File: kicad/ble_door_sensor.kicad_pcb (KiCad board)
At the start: 4 copper layers, 20 x 61.5 mm, 38 parts, among them J1 Prog Header, J101 Conn_01x08, SW101 SW_Reed, SW102 SW_Push, U1 nRF52832-QFxx, U101 TMP100, Y1 Crystal_GND24

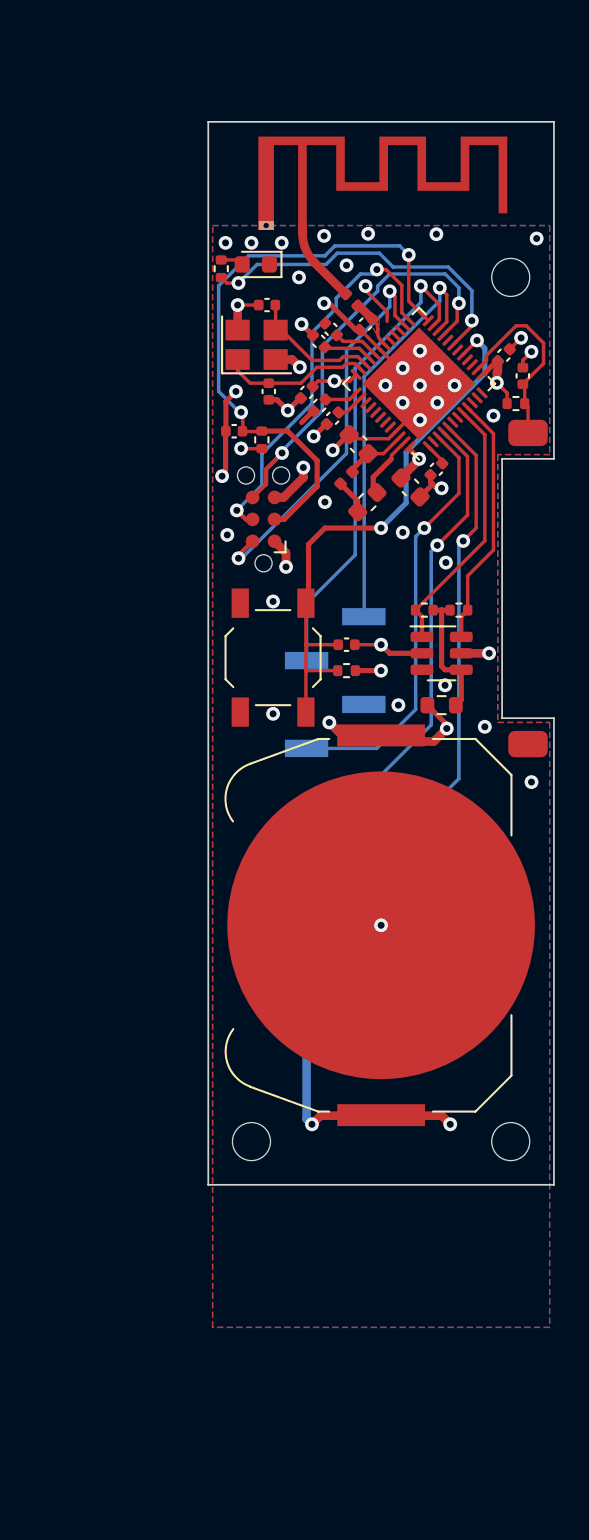
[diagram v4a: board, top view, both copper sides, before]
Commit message: Add tmp100 sensor for temperature
also added mounting holes for assembly machines
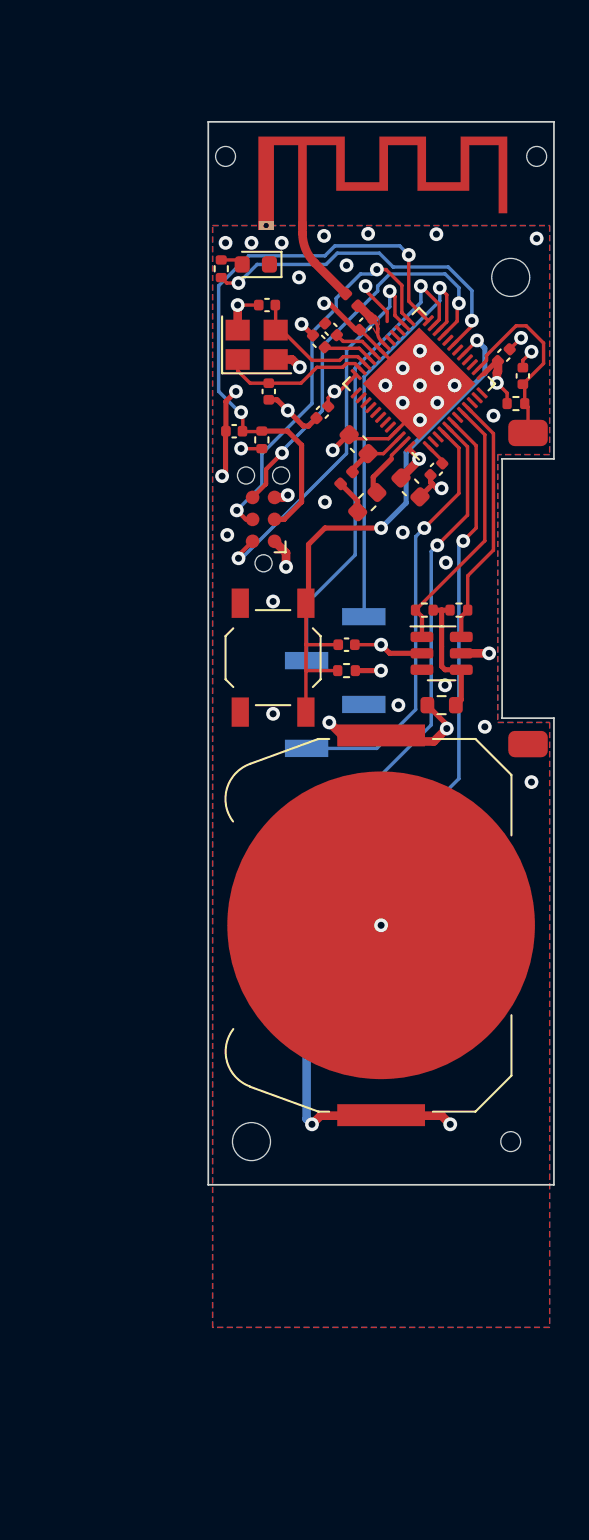
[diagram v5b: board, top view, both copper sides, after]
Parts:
- removed C105, C106: 12pF, Capacitor_SMD:C_0402_1005Metric
- removed H103: MountingHole, MountingHole:MountingHole_2.2mm_M2
- added T1: ToolingHole, Library:JLCPCB_Mounting_hole, F.Cu at (126.0, 42.0)
- added T2: ToolingHole, Library:JLCPCB_Mounting_hole, F.Cu at (142.5, 99.0)
- added T3: ToolingHole, Library:JLCPCB_Mounting_hole, F.Cu at (144.0, 42.0)
- moved C107 1.46 mm to (131.6, 56.8)
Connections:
- U1 pad 3: P0.01 -> unconnected-(U1-P0.01/XL2-Pad3)
- U1 pad 37: Net-(U1-P0.25) -> unconnected-(U1-P0.25-Pad37)
- U1 pad 38: Net-(U1-P0.26) -> unconnected-(U1-P0.26-Pad38)
- U1 pad 4: P0.02 -> P0.01
- U1 pad 5: P0.03 -> P0.02
- U1 pad 6: unconnected-(U1-P0.04/AIN2-Pad6) -> P0.03
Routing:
- net GND: track 66.2 -> 63.4 mm, vias 46 -> 45
- net Net-(U1-P0.25): track 1.93 -> 0.00 mm
- net Net-(U1-P0.26): track 1.65 -> 0.00 mm
- net RESET: track 35.3 -> 34.5 mm
- net P0.01: track 24.6 -> 25.2 mm

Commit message: Add ambient light and humidity sensor
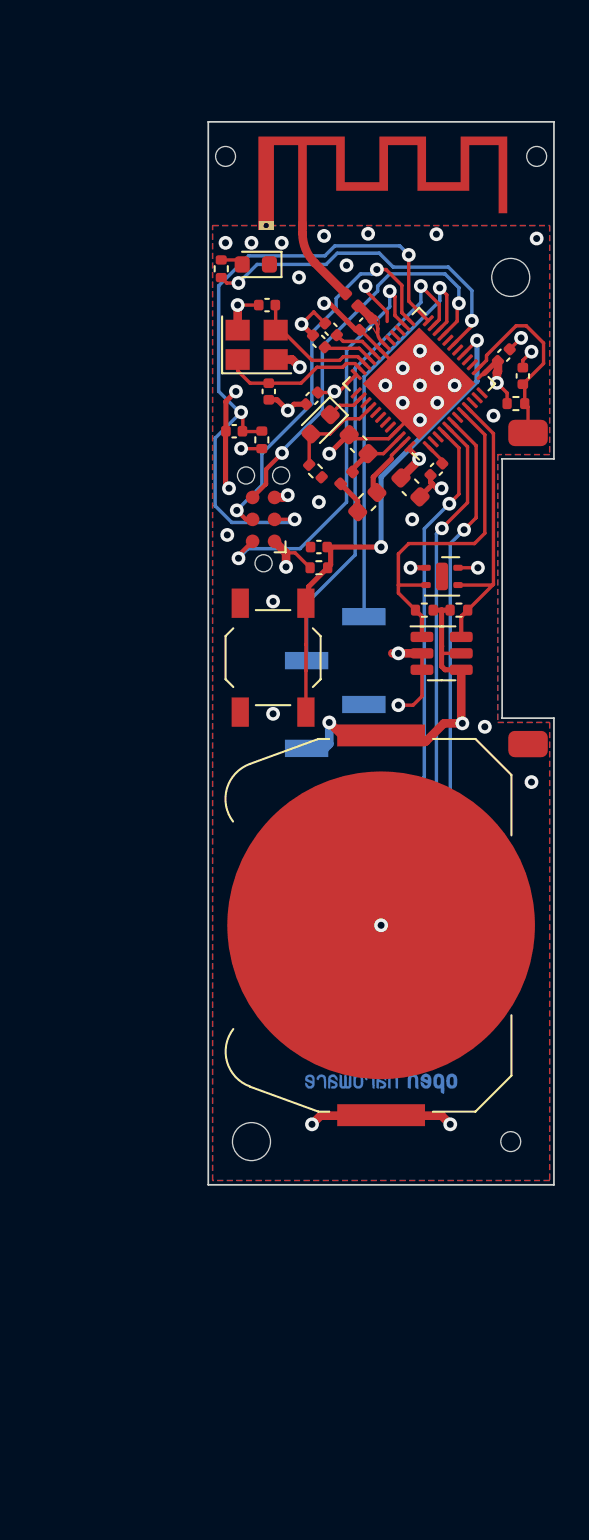
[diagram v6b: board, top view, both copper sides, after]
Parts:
- removed R103: 0, Resistor_SMD:R_0603_1608Metric
- added Q1: Photo, LED_SMD:LED_0603_1608Metric, F.Cu at (131.5, 57.5)
- added R3: 1K, Resistor_SMD:R_0402_1005Metric, F.Cu at (131.2, 60.2)
- added REF**: OSHW-Logo2_9.8x8mm_Copper, Symbol:OSHW-Logo2_9.8x8mm_Copper, B.Cu at (135.0, 92.5)
- added U2: SHTC3, Sensor_Humidity:Sensirion_DFN-4-1EP_2x2mm_P1mm_EP0.7x1.6mm, F.Cu at (138.5, 66.3)
- moved R101 6.16 mm to (131.4, 65.8), turned to 0 degrees
- moved C101 5.87 mm to (131.4, 64.6), turned to 180 degrees
- moved C107 1.00 mm to (131.0, 56.0)
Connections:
- J101 pad 4: P0.01 -> VCC
- J101 pad 5: P0.02 -> P0.01
- J101 pad 6: P0.03 -> P0.02
- J101 pad 7: GND -> P0.03
- J101 pad 8: VCC -> GND
- R104 pad 1: /VCC_Temp -> VCC
- R105 pad 1: /VCC_Temp -> VCC
- U1 pad 38: unconnected-(U1-P0.26-Pad38) -> /Photo_out
- U1 pad 40: unconnected-(U1-P0.28/AIN4-Pad40) -> /Photo_in
- U101 pad 4: /VCC_Temp -> VCC
- U101 pad 5: GND -> VCC
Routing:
- net GND: track 63.4 -> 71.2 mm, vias 45 -> 43
- net /VCC_Temp: track 7.63 -> 0.00 mm
- net P0.02: track 24.1 -> 31.1 mm
- net /Photo_in: track 0.00 -> 5.92 mm
- net SCL: track 15.3 -> 20.0 mm
- net RESET: track 34.5 -> 38.9 mm, vias 2 -> 3
- net BUTTON: track 32.8 -> 28.5 mm
- net /Photo_out: track 0.00 -> 2.19 mm
- net SDA: track 14.7 -> 16.7 mm
- net SWDIO: track 22.9 -> 24.5 mm
- net VCC: track 43.1 -> 44.1 mm

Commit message: Add MPN and Manufacturer for most parts
To be able to order from different houses
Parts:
- BT1: value Battery_Cell -> 3034
- Q1: value Photo -> ALS-PT19
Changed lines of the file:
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@@
     (tags "SMD SMT crystal")
     (property "LCSC#" "C9009")
+    (property "MPN" "X322532MOB4SI")
+    (property "Manufacturer" "YXC")
     (property "Sheetfile" "ble_door_sensor.kicad_sch")
     (property "Sheetname" "")
@@
     (tags "capacitor")
     (property "LCSC#" "C15195")
+    (property "MPN" "10nF 0402")
     (property "Sheetfile" "ble_door_sensor.kicad_sch")
     (property "Sheetname" "")
@@
   (footprint "Library:JLCPCB_Mounting_hole" (layer "F.Cu")
     (at 144 42)
+    (property "LCSC#" "-")
+    (property "MPN" "-")
     (property "Sheetfile" "ble_door_sensor.kicad_sch")
     (property "Sheetname" "")
+    (property "exclude_from_bom" "")
     (property "ki_description" "Mounting Hole without connection")
     (property "ki_keywords" "mounting hole")
+    (attr exclude_from_pos_files exclude_from_bom)
     (fp_text reference "T3" (at 0 -2.032 unlocked) (layer "F.SilkS") hide
         (effects (font (size 1 1) (thickness 0.1)))
@@
     (tags "mounting hole 2.2mm no annular m2")
     (property "LCSC#" "-")
+    (property "MPN" "-")
     (property "Sheetfile" "ble_door_sensor.kicad_sch")
     (property "Sheetname" "")
@@
     (tags "QFN NoLead")
     (property "LCSC#" "C77540")
+    (property "MPN" "NRF52832-QFAA-R")
+    (property "Manufacturer" "Nordic Semicon")
     (property "Sheetfile" "ble_door_sensor.kicad_sch")
     (property "Sheetname" "")
@@
     (tags "capacitor")
     (property "LCSC#" "C1525")
+    (property "MPN" "100nF 0402")
     (property "Sheetfile" "ble_door_sensor.kicad_sch")
     (property "Sheetname" "")
@@
     (tags "capacitor")
     (property "LCSC#" "C1546")
+    (property "MPN" "100pF 0402")
     (property "Sheetfile" "ble_door_sensor.kicad_sch")
     (property "Sheetname" "")
@@
     (tags "capacitor")
     (property "LCSC#" "C15849")
+    (property "MPN" "1uF 0603")
     (property "Sheetfile" "ble_door_sensor.kicad_sch")
     (property "Sheetname" "")
@@
     (at 143.5 67)
     (property "LCSC#" "-")
+    (property "MPN" "-")
     (property "Sheetfile" "ble_door_sensor.kicad_sch")
     (property "Sheetname" "")
@@
     (tags "inductor")
     (property "LCSC#" "C1035")
+    (property "MPN" "MLZ1608E100MT")
+    (property "Manufacturer" "TDK")
     (property "Sheetfile" "ble_door_sensor.kicad_sch")
     (property "Sheetname" "")
@@
     (tags "Keystone type 3034 coin cell retainer")
     (property "LCSC#" "C5213768")
+    (property "MPN" "3034TR")
+    (property "Manufacturer" "Keystone")
     (property "Sheetfile" "ble_door_sensor.kicad_sch")
     (property "Sheetname" "")
@@
         (effects (font (size 1 1) (thickness 0.15)))
     )
-    (fp_text value "Battery_Cell" (at 0 11.5 90) (layer "F.Fab")
+    (fp_text value "3034" (at 0 11.5 90) (layer "F.Fab")
         (effects (font (size 1 1) (thickness 0.15)))
     )
@@
     (tags "resistor")
     (property "LCSC#" "C11702")
+    (property "MPN" "1K")
     (property "Sheetfile" "ble_door_sensor.kicad_sch")
     (property "Sheetname" "")
@@
     (tags "capacitor")
     (property "LCSC#" "C1547")
+    (property "MPN" "12pF 0402")
     (property "Sheetfile" "ble_door_sensor.kicad_sch")
     (property "Sheetname" "")
@@
     (tags "resistor")
     (property "LCSC#" "C11702")
+    (property "MPN" "1K")
     (property "Sheetfile" "ble_door_sensor.kicad_sch")
     (property "Sheetname" "")
@@
     (tags "LED")
     (property "LCSC#" "C72043")
+    (property "MPN" " KP-1608SGC")
     (property "Sheetfile" "ble_door_sensor.kicad_sch")
     (property "Sheetname" "")
@@
     (tags "resistor")
     (property "LCSC#" "C25741")
+    (property "MPN" "100K")
     (property "Sheetfile" "ble_door_sensor.kicad_sch")
     (property "Sheetname" "")
@@
     (tags "mounting hole 2.2mm no annular m2")
     (property "LCSC#" "-")
+    (property "MPN" "-")
     (property "Sheetfile" "ble_door_sensor.kicad_sch")
     (property "Sheetname" "")
@@
     (tags "Sensirion DFN NoLead")
     (property "LCSC#" "C2880044")
+    (property "MPN" "SHTC3-TR-10KS")
+    (property "Manufacturer" "Sensirion")
     (property "Sheetfile" "ble_door_sensor.kicad_sch")
     (property "Sheetname" "")
@@
     (tags "resistor")
     (property "LCSC#" "C26083")
+    (property "MPN" "1M")
     (property "Sheetfile" "ble_door_sensor.kicad_sch")
     (property "Sheetname" "")
@@
     (tags "resistor")
     (property "LCSC#" "C25741")
+    (property "MPN" "100K")
     (property "Sheetfile" "ble_door_sensor.kicad_sch")
     (property "Sheetname" "")
@@
     (tags "capacitor")
     (property "LCSC#" "C1525")
+    (property "MPN" "100nF 0402")
     (property "Sheetfile" "ble_door_sensor.kicad_sch")
     (property "Sheetname" "")
@@
     (tags "capacitor")
     (property "LCSC#" "-")
+    (property "MPN" "-")
     (property "Sheetfile" "ble_door_sensor.kicad_sch")
     (property "Sheetname" "")
@@
     (property "ki_description" "Unpolarized capacitor, small symbol")
     (property "ki_keywords" "capacitor cap")
-    (attr smd exclude_from_bom)
+    (attr smd exclude_from_pos_files exclude_from_bom)
     (fp_text reference "C4" (at 0 -1.16 45) (layer "F.SilkS") hide
         (effects (font (size 1 1) (thickness 0.15)))
@@
     (tags "capacitor")
     (property "LCSC#" "C1525")
+    (property "MPN" "100nF 0402")
     (property "Sheetfile" "ble_door_sensor.kicad_sch")
     (property "Sheetname" "")
@@
     (tags "PCB antenna")
     (property "LCSC#" "-")
+    (property "MPN" "-")
     (property "Sheetfile" "ble_door_sensor.kicad_sch")
     (property "Sheetname" "")
@@
     (tags "SOT TO_SOT_SMD")
     (property "LCSC#" "C31810")
+    (property "MPN" "TMP100NA/3K")
+    (property "Manufacturer" "Texas Instruments")
     (property "Sheetfile" "ble_door_sensor.kicad_sch")
     (property "Sheetname" "")
@@
     (tags "capacitor")
     (property "LCSC#" "C1546")
+    (property "MPN" "100pF 0402")
     (property "Sheetfile" "ble_door_sensor.kicad_sch")
     (property "Sheetname" "")
@@
   (footprint "Library:JLCPCB_Mounting_hole" (layer "F.Cu")
     (at 142.5 99)
+    (property "LCSC#" "-")
+    (property "MPN" "-")
     (property "Sheetfile" "ble_door_sensor.kicad_sch")
     (property "Sheetname" "")
+    (property "exclude_from_bom" "")
     (property "ki_description" "Mounting Hole without connection")
     (property "ki_keywords" "mounting hole")
+    (attr exclude_from_pos_files exclude_from_bom)
     (fp_text reference "T2" (at 0 -2.032 unlocked) (layer "F.SilkS") hide
         (effects (font (size 1 1) (thickness 0.1)))
@@
     (tags "SPST Tactile Switch")
     (property "LCSC#" "C318884")
+    (property "MPN" "TS-1187A-B-A-B")
+    (property "Manufacturer" "XKB Connectivity")
     (property "Sheetfile" "ble_door_sensor.kicad_sch")
     (property "Sheetname" "")
@@
     (tags "capacitor")
     (property "LCSC#" "C1547")
+    (property "MPN" "12pF 0402")
     (property "Sheetfile" "ble_door_sensor.kicad_sch")
     (property "Sheetname" "")
@@
     (tags "tag connect programming header pogo pins")
     (property "LCSC#" "-")
+    (property "MPN" "-")
     (property "Sheetfile" "ble_door_sensor.kicad_sch")
     (property "Sheetname" "")
@@
     (descr "LED SMD 0603 (1608 Metric), square (rectangular) end terminal, IPC_7351 nominal, (Body size source: http://www.tortai-tech.com/upload/download/2011102023233369053.pdf), generated with kicad-footprint-generator")
     (tags "LED")
+    (property "LCSC#" "C146233")
+    (property "MPN" "ALS-PT19-315C/L177/TR8")
     (property "Sheetfile" "ble_door_sensor.kicad_sch")
     (property "Sheetname" "")
@@
         (effects (font (size 1 1) (thickness 0.15)))
     )
-    (fp_text value "Photo" (at 0 1.43 45) (layer "F.Fab")
+    (fp_text value "ALS-PT19" (at 0 1.43 45) (layer "F.Fab")
         (effects (font (size 1 1) (thickness 0.15)))
     )
@@
     (tags "resistor")
     (property "LCSC#" "C25741")
+    (property "MPN" "100K")
     (property "Sheetfile" "ble_door_sensor.kicad_sch")
     (property "Sheetname" "")
@@
   (footprint "Library:JLCPCB_Mounting_hole" (layer "F.Cu")
     (at 126 42)
+    (property "LCSC#" "-")
+    (property "MPN" "-")
     (property "Sheetfile" "ble_door_sensor.kicad_sch")
     (property "Sheetname" "")
+    (property "exclude_from_bom" "")
     (property "ki_description" "Mounting Hole without connection")
     (property "ki_keywords" "mounting hole")
+    (attr exclude_from_pos_files exclude_from_bom)
     (fp_text reference "T1" (at 0 -2.032 unlocked) (layer "F.SilkS") hide
         (effects (font (size 1 1) (thickness 0.1)))
@@
     (tags "resistor")
     (property "LCSC#" "C25741")
+    (property "MPN" "100K")
     (property "Sheetfile" "ble_door_sensor.kicad_sch")
     (property "Sheetname" "")
@@
     (tags "capacitor")
     (property "LCSC#" "C1525")
+    (property "MPN" "100nF 0402")
     (property "Sheetfile" "ble_door_sensor.kicad_sch")
     (property "Sheetname" "")
@@
     (tags "inductor")
     (property "LCSC#" "C27143")
+    (property "MPN" "LQW15AN15NH00D")
+    (property "Manufacturer" "Murata Electronics")
     (property "Sheetfile" "ble_door_sensor.kicad_sch")
     (property "Sheetname" "")
@@
     (tags "inductor")
     (property "LCSC#" "C14033")
+    (property "MPN" "LQG15HS3N3C02D")
+    (property "Manufacturer" "Murata Electronics")
     (property "Sheetfile" "ble_door_sensor.kicad_sch")
     (property "Sheetname" "")
@@
     (tags "capacitor")
     (property "LCSC#" "C19666")
+    (property "MPN" "4,7uF 0603")
     (property "Sheetfile" "ble_door_sensor.kicad_sch")
     (property "Sheetname" "")
@@
     (tags "capacitor")
     (property "LCSC#" "C1525")
+    (property "MPN" "100nF 0402")
     (property "Sheetfile" "ble_door_sensor.kicad_sch")
     (property "Sheetname" "")
@@
     (tags "Surface mounted pin header SMD 1x08 2.54mm single row style1 pin1 left")
     (property "LCSC#" "-")
+    (property "MPN" "-")
     (property "Sheetfile" "ble_door_sensor.kicad_sch")
     (property "Sheetname" "")

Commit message: Update to Kicad 8
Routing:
- net GND: track 71.2 -> 74.0 mm
